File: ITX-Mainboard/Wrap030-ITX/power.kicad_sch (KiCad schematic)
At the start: 25 parts, among them J7 ATX-24, J8 Conn_01x02, P8 Conn_01x06, P9 Conn_01x06, Q1 PN2222A

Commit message: Completing PCB Routing
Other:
- title: Wrap030 ITX -> Wrap030-ATX Mainboard
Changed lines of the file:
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@@
   (paper "USLetter")
   (title_block
-    (title "Wrap030 ITX")
-    (date "2023-03-15")
-    (rev "0")
+    (title "Wrap030-ATX Mainboard")
+    (date "2023-03-26")
+    (rev "1")
     (company "techav")
   )

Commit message: PCB Silkscreen & DRC Cleanup
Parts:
- added FID1, FID2, FID3: Fiducial, Fiducial:Fiducial_1mm_Mask2mm, symbol Mechanical:Fiducial
- J8: value Conn_01x02 -> POWER
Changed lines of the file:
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@@
+    )
+  )
+  (symbol (lib_id "Mechanical:Fiducial") (at 228.6 63.5 0) (unit 1)
+    (in_bom yes) (on_board yes) (dnp no) (fields_autoplaced)
+    (property "Reference" "FID2" (at 230.759 62.8563 0)
+      (effects (font (size 1.27 1.27)) (justify left))
+    )
+    (property "Value" "Fiducial" (at 230.759 64.7773 0)
+      (effects (font (size 1.27 1.27)) (justify left))
+    )
+    (property "Footprint" "Fiducial:Fiducial_1mm_Mask2mm" (at 228.6 63.5 0)
+      (effects (font (size 1.27 1.27)) hide)
+    )
+    (property "Datasheet" "~" (at 228.6 63.5 0)
+      (effects (font (size 1.27 1.27)) hide)
+    )
+    (instances
+      (project "Wrap030-ITX"
+        (path "/911cb688-7d4c-4194-bbd3-2b645bd8d53c/e0e7274a-05f5-4d4a-be10-b5428e1556d7"
+          (reference "FID2") (unit 1)
+        )
+      )
     )
   )
@@
     )
   )
+  (symbol (lib_id "Mechanical:Fiducial") (at 241.3 63.5 0) (unit 1)
+    (in_bom yes) (on_board yes) (dnp no) (fields_autoplaced)
+    (property "Reference" "FID3" (at 243.459 62.8563 0)
+      (effects (font (size 1.27 1.27)) (justify left))
+    )
+    (property "Value" "Fiducial" (at 243.459 64.7773 0)
+      (effects (font (size 1.27 1.27)) (justify left))
+    )
+    (property "Footprint" "Fiducial:Fiducial_1mm_Mask2mm" (at 241.3 63.5 0)
+      (effects (font (size 1.27 1.27)) hide)
+    )
+    (property "Datasheet" "~" (at 241.3 63.5 0)
+      (effects (font (size 1.27 1.27)) hide)
+    )
+    (instances
+      (project "Wrap030-ITX"
+        (path "/911cb688-7d4c-4194-bbd3-2b645bd8d53c/e0e7274a-05f5-4d4a-be10-b5428e1556d7"
+          (reference "FID3") (unit 1)
+        )
+      )
+    )
+  )
   (symbol (lib_id "power:-12V") (at 104.14 60.96 270) (unit 1)
     (in_bom yes) (on_board yes) (dnp no) (fields_autoplaced)
@@
       (effects (font (size 1.27 1.27)) (justify left))
     )
-    (property "Value" "Conn_01x02" (at 53.848 40.6473 0)
+    (property "Value" "POWER" (at 53.848 40.6473 0)
       (effects (font (size 1.27 1.27)) (justify left))
     )
@@
         )
       )
+    )
+  )
+  (symbol (lib_id "Mechanical:Fiducial") (at 215.9 63.5 0) (unit 1)
+    (in_bom yes) (on_board yes) (dnp no) (fields_autoplaced)
+    (property "Reference" "FID1" (at 218.059 62.8563 0)
+      (effects (font (size 1.27 1.27)) (justify left))
+    )
+    (property "Value" "Fiducial" (at 218.059 64.7773 0)
+      (effects (font (size 1.27 1.27)) (justify left))
+    )
+    (property "Footprint" "Fiducial:Fiducial_1mm_Mask2mm" (at 215.9 63.5 0)
+      (effects (font (size 1.27 1.27)) hide)
+    )
+    (property "Datasheet" "~" (at 215.9 63.5 0)
+      (effects (font (size 1.27 1.27)) hide)
+    )
+    (instances
+      (project "Wrap030-ITX"
+        (path "/911cb688-7d4c-4194-bbd3-2b645bd8d53c/e0e7274a-05f5-4d4a-be10-b5428e1556d7"
+          (reference "FID1") (unit 1)
+        )
+      )

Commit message: initial production schematic
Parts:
- P8: value Conn_01x06 -> AT-P8
- P9: value Conn_01x06 -> AT-P9
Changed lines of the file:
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@@
       (effects (font (size 1.27 1.27)) (justify left))
     )
-    (property "Value" "Conn_01x06" (at 102.362 86.3673 0)
+    (property "Value" "AT-P8" (at 102.362 86.3673 0)
       (effects (font (size 1.27 1.27)) (justify left))
     )
@@
       (effects (font (size 1.27 1.27)) (justify left))
     )
-    (property "Value" "Conn_01x06" (at 102.362 101.6073 0)
-      (effects (font (size 1.27 1.27)) (justify left))
-    )
+    (property "Value" "AT-P9" (at 102.362 101.6073 0)
+      (effects (font (size 1.27 1.27)) (justify left))
+    )

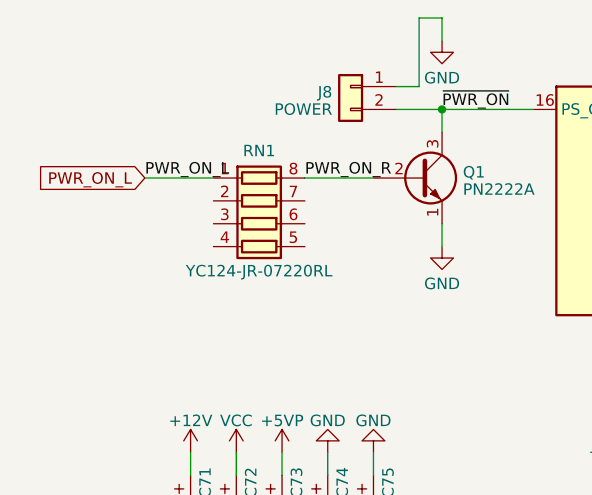
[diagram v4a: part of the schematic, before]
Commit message: Replace resistor nets with 0402 & update gerbers
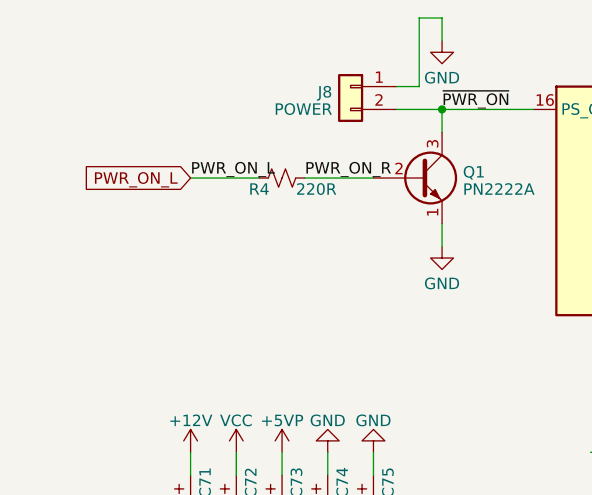
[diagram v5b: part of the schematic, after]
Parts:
- removed RN1: YC124-JR-07220RL, Resistor_SMD:R_Array_Convex_4x1206, symbol Device:R_Pack04
- added R4: 220R, Resistor_SMD:R_0402_1005Metric_Pad0.72x0.64mm_HandSolder, symbol Device:R_Small_US
- C71, C72, C73, C74, C75: Mouser-Part (none) -> 710-860010372001; Notes (none) -> OFE
- C83, C84, C85, C86, C87: Mouser-Part (none) -> 710-860010473007; Notes (none) -> OFE
- FID1, FID2, FID3, H1, H2, H3, H4, H5, H6, H7, H8, H9: Notes (none) -> NA
- J7: Mouser-Part (none) -> 538-39-28-8240
- J8: Mouser-Part (none) -> 523-G800NA306018EU; Notes (none) -> OFE
- P8, P9: Mouser-Part (none) -> 538-26-60-4060; Notes (none) -> OFE
- Q1: Mouser-Part (none) -> 512-PN2222ABU; Notes (none) -> OFE
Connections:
- net PWR_ON_L: now also R4.1
- net PWR_ON_R: now also R4.2
